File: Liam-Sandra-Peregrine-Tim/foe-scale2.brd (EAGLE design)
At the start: 96.2 x 67.3 mm, 52 parts, among them U1 LM311, U2 SAMD21E

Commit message: fixed up a couple things in board
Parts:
- added R18: 0, resistor:R0805
- moved DGND 18.0 mm to (58.4, 17.8)
- moved U$5 5.68 mm to (58.4, 36.8)
- moved U$4 2.54 mm to (64.8, 36.8)
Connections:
- net AGND: now also R18.2
- net DGND: now also R18.1
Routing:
- net +5V: track 274.7 -> 284.8 mm
- net AGND: track 65.9 -> 72.0 mm, vias 12 -> 13
- net DBG-PIN-PA14: track 5.98 -> 11.6 mm
- net DGND: track 76.8 -> 80.6 mm, vias 14 -> 15
- net RST: track 44.7 -> 44.1 mm

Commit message: pushing
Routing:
- net N$70: track 8.86 -> 11.5 mm
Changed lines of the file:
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@@
 </class>
 </classes>
-<designrules name="default">
+<designrules name="default *">
 <description language="de">&lt;b&gt;EAGLE Design Rules&lt;/b&gt;
 &lt;p&gt;
@@
 <param name="mtCopper" value="0.035mm 0.035mm 0.035mm 0.035mm 0.035mm 0.035mm 0.035mm 0.035mm 0.035mm 0.035mm 0.035mm 0.035mm 0.035mm 0.035mm 0.035mm 0.035mm"/>
 <param name="mtIsolate" value="1.5mm 0.15mm 0.2mm 0.15mm 0.2mm 0.15mm 0.2mm 0.15mm 0.2mm 0.15mm 0.2mm 0.15mm 0.2mm 0.15mm 0.2mm"/>
-<param name="mdWireWire" value="8mil"/>
-<param name="mdWirePad" value="8mil"/>
-<param name="mdWireVia" value="8mil"/>
-<param name="mdPadPad" value="8mil"/>
-<param name="mdPadVia" value="8mil"/>
-<param name="mdViaVia" value="8mil"/>
-<param name="mdSmdPad" value="8mil"/>
-<param name="mdSmdVia" value="8mil"/>
-<param name="mdSmdSmd" value="8mil"/>
+<param name="mdWireWire" value="6mil"/>
+<param name="mdWirePad" value="6mil"/>
+<param name="mdWireVia" value="6mil"/>
+<param name="mdPadPad" value="6mil"/>
+<param name="mdPadVia" value="6mil"/>
+<param name="mdViaVia" value="6mil"/>
+<param name="mdSmdPad" value="6mil"/>
+<param name="mdSmdVia" value="6mil"/>
+<param name="mdSmdSmd" value="6mil"/>
 <param name="mdViaViaSameLayer" value="8mil"/>
 <param name="mnLayersViaInSmd" value="2"/>
 <param name="mdCopperDimension" value="40mil"/>
-<param name="mdDrill" value="8mil"/>
+<param name="mdDrill" value="6mil"/>
 <param name="mdSmdStop" value="0mil"/>
 <param name="msWidth" value="10mil"/>
@@
 </element>
 <element name="R11" library="resistor" package="R0805" value="10k" x="63.5" y="76.2" smashed="yes" rot="R180">
-<attribute name="NAME" x="60.833" y="75.438" size="1.27" layer="25" rot="R270"/>
+<attribute name="NAME" x="60.671525" y="75.39493125" size="1.27" layer="25" rot="R270"/>
 <attribute name="VALUE" x="61.849" y="78.232" size="1.27" layer="27"/>
 </element>
@@
 <wire x1="37.973" y1="41.275" x2="37.846" y2="41.402" width="0.4064" layer="1"/>
 <wire x1="37.846" y1="41.402" x2="37.846" y2="42.164" width="0.4064" layer="1"/>
-<wire x1="37.846" y1="42.164" x2="35.56" y2="44.45" width="0.4064" layer="1"/>
-<wire x1="35.56" y1="44.45" x2="32.512" y2="44.45" width="0.4064" layer="1"/>
-<wire x1="32.512" y1="44.45" x2="29.718" y2="47.244" width="0.4064" layer="1"/>
+<wire x1="37.846" y1="42.164" x2="35.549234375" y2="44.633034375" width="0.4064" layer="1"/>
+<wire x1="35.549234375" y1="44.633034375" x2="32.501234375" y2="44.633034375" width="0.4064" layer="1"/>
+<wire x1="32.501234375" y1="44.633034375" x2="29.718" y2="47.244" width="0.4064" layer="1"/>
 <wire x1="29.718" y1="47.244" x2="29.718" y2="49.276" width="0.4064" layer="1"/>
 <wire x1="29.718" y1="49.276" x2="22.606" y2="56.388" width="0.4064" layer="1"/>
@@
 <contactref element="U2" pad="3"/>
 <wire x1="30.16" y1="59.69" x2="30.48" y2="59.69" width="0.4064" layer="1"/>
-<wire x1="74.86" y1="48.1076" x2="74.86" y2="46.92" width="0.4064" layer="1"/>
-<wire x1="74.86" y1="46.92" x2="73.66" y2="45.72" width="0.4064" layer="1"/>
-<via x="73.66" y="45.72" extent="1-16" drill="0.6"/>
-<wire x1="73.66" y1="45.72" x2="71.12" y2="45.72" width="0.4064" layer="16"/>
-<wire x1="71.12" y1="45.72" x2="69.088" y2="47.752" width="0.4064" layer="16"/>
+<wire x1="74.86" y1="48.1076" x2="74.816940625" y2="46.672365625" width="0.4064" layer="1"/>
+<wire x1="74.816940625" y1="46.672365625" x2="73.616940625" y2="45.472365625" width="0.4064" layer="1"/>
+<via x="73.616940625" y="45.472365625" extent="1-16" drill="0.6"/>
+<wire x1="73.616940625" y1="45.472365625" x2="71.173825" y2="45.48313125" width="0.4064" layer="16"/>
+<wire x1="71.173825" y1="45.48313125" x2="69.088" y2="47.752" width="0.4064" layer="16"/>
 <via x="69.088" y="47.752" extent="1-16" drill="0.6"/>
 <wire x1="69.088" y1="47.752" x2="68.072" y2="47.752" width="0.4064" layer="1"/>
@@
 <contactref element="R12" pad="2"/>
 <contactref element="AS1363" pad="2"/>
-<wire x1="66.04" y1="72.27" x2="66.04" y2="72.898" width="0.4064" layer="1"/>
-<wire x1="66.04" y1="72.898" x2="65.278" y2="73.66" width="0.4064" layer="1"/>
-<via x="65.278" y="73.66" extent="1-16" drill="0.6"/>
-<wire x1="65.278" y1="73.66" x2="65.278" y2="74.168" width="0.4064" layer="16"/>
+<wire x1="66.04" y1="72.27" x2="66.06233125" y2="73.724378125" width="0.4064" layer="1"/>
+<wire x1="66.06233125" y1="73.724378125" x2="64.008" y2="73.66" width="0.4064" layer="1"/>
+<via x="64.008" y="73.66" extent="1-16" drill="0.6"/>
+<wire x1="64.008" y1="73.66" x2="65.278" y2="74.168" width="0.4064" layer="16"/>
 <wire x1="65.278" y1="74.168" x2="66.04" y2="74.93" width="0.4064" layer="16"/>
 <wire x1="66.04" y1="74.93" x2="66.294" y2="76.454" width="0.4064" layer="16"/>

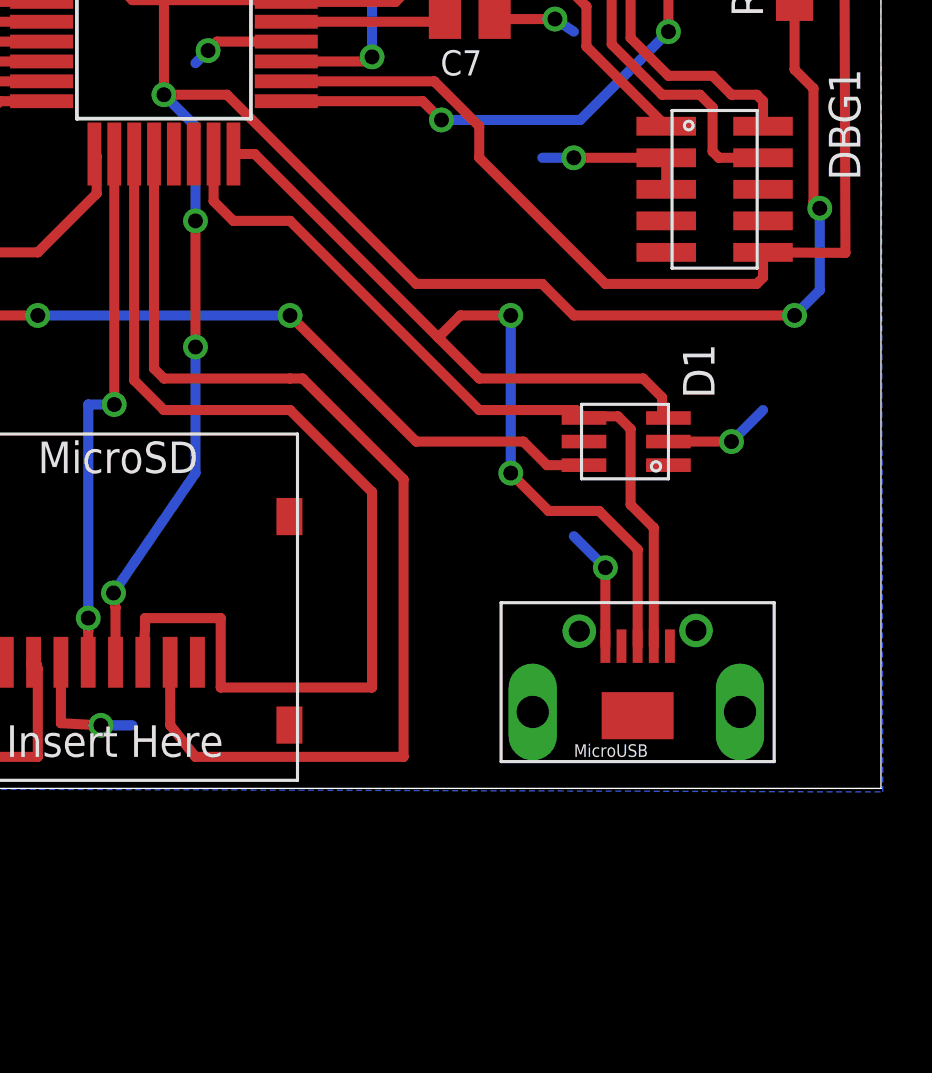
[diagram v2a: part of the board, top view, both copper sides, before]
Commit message: replaced microUSB with standard USB B
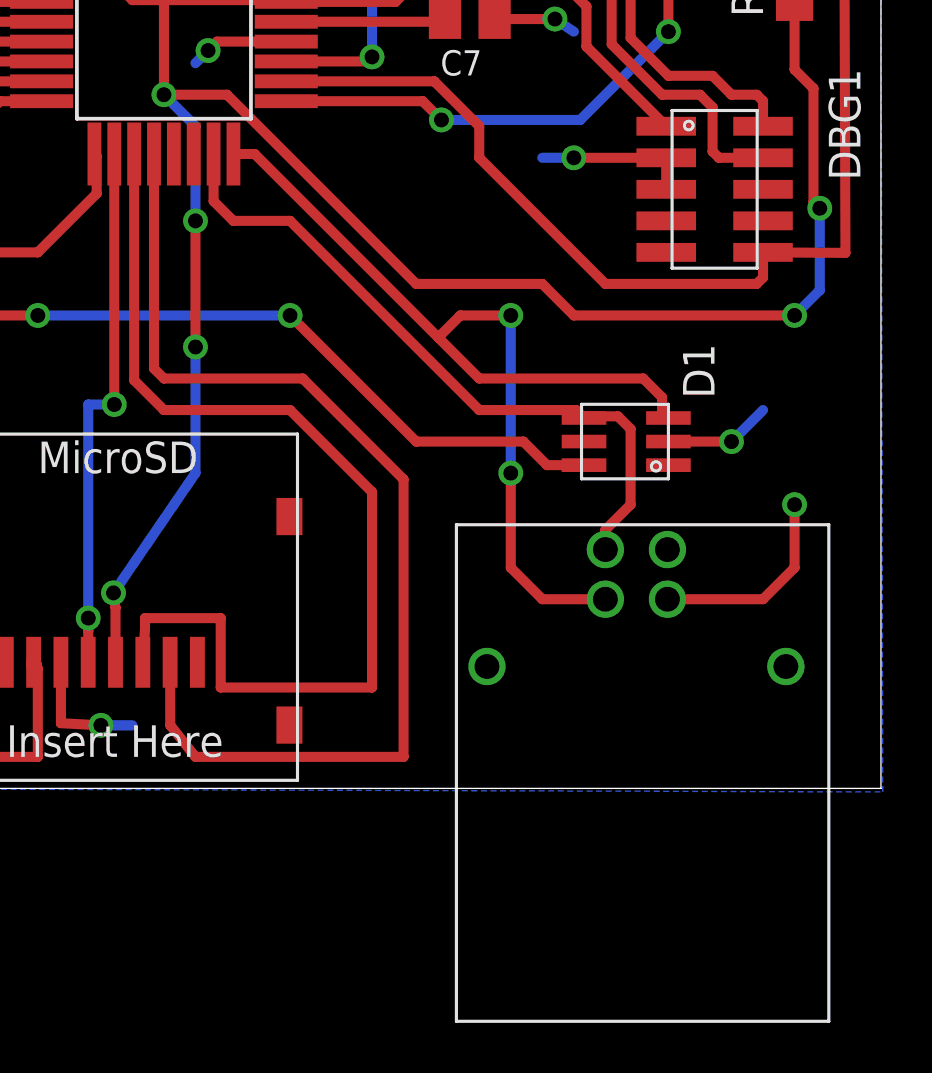
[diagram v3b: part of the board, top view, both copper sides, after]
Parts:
- U$13: value MICRO-USB-CONNECTOR -> USB-B; device foe-scale:MICRO-USB-CONNECTOR -> foe-scale:USB-B
- moved U$13 2.54 mm to (91.4, 20.3)
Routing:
- net USB_D-_PA24: track 31.7 -> 27.8 mm
- net DGND: track 80.6 -> 83.9 mm
- net USB_D+_PA25: track 42.2 -> 40.0 mm
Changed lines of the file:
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@@
 <?xml version="1.0" encoding="utf-8"?>
 <!DOCTYPE eagle SYSTEM "eagle.dtd">
-<eagle version="7.4.0">
+<eagle version="7.5.0">
 <drawing>
 <settings>
@@
 Shifter</text>
 <text x="62.23" y="16.51" size="1.778" layer="27" rot="R90">MicroSD</text>
-<text x="100.838" y="13.716" size="1.778" layer="27" rot="R90">MicroUSB</text>
+<text x="102.108" y="13.716" size="1.778" layer="27" rot="R90">MicroUSB</text>
 </plain>
 <attributes>
@@
 <element name="U$11" library="foe-scale" package="PUSHBTN" value="BUTTON_THRU" x="92.71" y="55.88" rot="R270"/>
 <element name="U$12" library="foe-scale" package="PUSHBTN" value="BUTTON_THRU" x="92.71" y="69.85" rot="R270"/>
-<element name="U$13" library="foe-scale" package="MICRO-USB-CONNECTOR" value="MICRO-USB-CONNECTOR" x="91.44" y="17.78"/>
+<element name="U$13" library="foe-scale" package="USB-B" value="USB-B" x="91.44" y="20.32"/>
 <element name="U$2" library="foe-scale" package="S8-LT1789-1" value="LT1789-1-INSTR-AMP" x="15.24" y="45.72" smashed="yes" rot="R270"/>
 <element name="U$3" library="foe-scale" package="SOIC8" value="LMC6482" x="36.83" y="41.91" smashed="yes" rot="R270">
@@
 <via x="96.52" y="26.67" extent="1-16" drill="0.6"/>
 <wire x1="96.52" y1="26.67" x2="97.79" y2="27.94" width="0.4064" layer="16"/>
-<wire x1="91.44" y1="18.43" x2="91.44" y2="21.59" width="0.4064" layer="1"/>
-<via x="91.44" y="21.59" extent="1-16" drill="0.6"/>
-<wire x1="91.44" y1="21.59" x2="90.17" y2="22.86" width="0.4064" layer="16"/>
+<via x="99.06" y="24.13" extent="1-16" drill="0.6"/>
 <wire x1="93.89" y1="36.83" x2="93.89" y2="38.1" width="0.4064" layer="1"/>
 <wire x1="93.89" y1="38.1" x2="90.17" y2="38.1" width="0.4064" layer="1"/>
@@
 <via x="58.42" y="66.04" extent="1-16" drill="0.6"/>
 <wire x1="58.42" y1="66.04" x2="58.42" y2="64.77" width="0.6096" layer="16"/>
+<wire x1="93.94" y1="20.32" x2="97.79" y2="20.32" width="0.4064" layer="1"/>
+<wire x1="97.79" y1="20.32" x2="99.06" y2="21.59" width="0.4064" layer="1"/>
+<wire x1="99.06" y1="21.59" x2="99.06" y2="24.13" width="0.4064" layer="1"/>
+<wire x1="87.63" y1="69.85" x2="97.7138" y2="74.8538" width="0" layer="19" extent="16-16"/>
+<wire x1="78.74" y1="73.66" x2="84.82" y2="68.58" width="0" layer="19" extent="1-16"/>
+<wire x1="65.09" y1="69.97" x2="74.93" y2="75.2" width="0" layer="19" extent="1-1"/>
+<wire x1="59.69" y1="67.31" x2="62.23" y2="68.58" width="0" layer="19" extent="16-16"/>
+<wire x1="58.42" y1="66.04" x2="59.69" y2="67.31" width="0" layer="19" extent="1-16"/>
+<wire x1="58.42" y1="55.88" x2="58.42" y2="64.77" width="0" layer="19" extent="16-16"/>
+<wire x1="54.035" y1="47.565" x2="56.300771875" y2="53.63770625" width="0" layer="19" extent="1-1"/>
+<wire x1="66.04" y1="45.72" x2="59.69" y2="40.64" width="0" layer="19" extent="1-16"/>
+<wire x1="74.93" y1="41.91" x2="68.7324" y2="45.18" width="0" layer="19" extent="1-16"/>
+<wire x1="86.979" y1="43.688" x2="78.5876" y2="42.78" width="0" layer="19" extent="1-1"/>
+<wire x1="90.17" y1="38.1" x2="90.17" y2="43.18" width="0" layer="19" extent="1-16"/>
+<wire x1="97.79" y1="27.94" x2="93.89" y2="36.83" width="0" layer="19" extent="1-16"/>
+<wire x1="99.06" y1="24.13" x2="96.52" y2="26.67" width="0" layer="19" extent="16-16"/>
+<wire x1="59.69" y1="29.21" x2="59.69" y2="40.64" width="0" layer="19" extent="16-16"/>
+<wire x1="58.42" y1="17.78" x2="59.0032625" y2="28.5232625" width="0" layer="19" extent="1-1"/>
+<wire x1="69.51" y1="17.78" x2="58.42" y2="17.78" width="0" layer="19" extent="1-1"/>
+<wire x1="99.06" y1="50.53" x2="90.17" y2="43.18" width="0" layer="19" extent="1-16"/>
+<wire x1="97.7138" y1="60.8838" x2="100.33" y2="54.61" width="0" layer="19" extent="16-16"/>
 </signal>
 <signal name="DO-PA16">
@@
 <contactref element="U$8" pad="CD"/>
 <contactref element="U2" pad="20"/>
-<wire x1="73.26" y1="38.2524" x2="73.26" y2="29.972" width="0.4064" layer="1"/>
-<wire x1="73.26" y1="29.972" x2="73.26" y2="29.61" width="0.4064" layer="1"/>
+<wire x1="73.26" y1="38.2524" x2="73.26" y2="29.61" width="0.4064" layer="1"/>
 <wire x1="73.26" y1="29.61" x2="73.66" y2="29.21" width="0.4064" layer="1"/>
-<wire x1="73.66" y1="29.21" x2="78.74" y2="29.21" width="0.4064" layer="1"/>
-<wire x1="78.74" y1="29.21" x2="79.248" y2="29.21" width="0.4064" layer="1"/>
+<wire x1="73.66" y1="29.21" x2="79.248" y2="29.21" width="0.4064" layer="1"/>
 <wire x1="79.248" y1="29.21" x2="83.312" y2="25.146" width="0.4064" layer="1"/>
 <wire x1="83.312" y1="25.146" x2="83.312" y2="13.97" width="0.4064" layer="1"/>
@@
 <wire x1="86.36" y1="27.94" x2="90.26" y2="27.94" width="0.4064" layer="1"/>
 <wire x1="90.26" y1="27.94" x2="90.58" y2="27.62" width="0.4064" layer="1"/>
-<wire x1="93.39" y1="18.43" x2="93.39" y2="23.196" width="0.4064" layer="1"/>
-<wire x1="93.39" y1="23.196" x2="92.456" y2="24.13" width="0.4064" layer="1"/>
 <wire x1="92.456" y1="24.13" x2="92.456" y2="27.178" width="0.4064" layer="1"/>
 <wire x1="92.456" y1="27.178" x2="91.948" y2="27.686" width="0.4064" layer="1"/>
 <wire x1="91.948" y1="27.686" x2="90.646" y2="27.686" width="0.4064" layer="1"/>
 <wire x1="90.646" y1="27.686" x2="90.58" y2="27.62" width="0.4064" layer="1"/>
+<wire x1="91.44" y1="22.32" x2="91.44" y2="23.114" width="0.4064" layer="1"/>
+<wire x1="91.44" y1="23.114" x2="92.456" y2="24.13" width="0.4064" layer="1"/>
 </signal>
 <signal name="USB_D+_PA25">
@@
 <wire x1="93.726" y1="28.448" x2="93.726" y2="27.874" width="0.4064" layer="1"/>
 <wire x1="93.726" y1="27.874" x2="93.98" y2="27.62" width="0.4064" layer="1"/>
-<wire x1="92.74" y1="18.43" x2="92.74" y2="22.322" width="0.4064" layer="1"/>
-<wire x1="92.74" y1="22.322" x2="91.186" y2="23.876" width="0.4064" layer="1"/>
-<wire x1="91.186" y1="23.876" x2="89.154" y2="23.876" width="0.4064" layer="1"/>
-<wire x1="89.154" y1="23.876" x2="87.63" y2="25.4" width="0.4064" layer="1"/>
 <via x="87.63" y="25.4" extent="1-16" drill="0.6"/>
 <wire x1="87.63" y1="25.4" x2="87.63" y2="31.75" width="0.4064" layer="16"/>
@@
 <wire x1="87.63" y1="31.75" x2="85.598" y2="31.75" width="0.4064" layer="1"/>
 <wire x1="85.598" y1="31.75" x2="84.709" y2="30.861" width="0.4064" layer="1"/>
+<wire x1="91.44" y1="20.32" x2="88.9" y2="20.32" width="0.4064" layer="1"/>
+<wire x1="88.9" y1="20.32" x2="87.63" y2="21.59" width="0.4064" layer="1"/>
+<wire x1="87.63" y1="21.59" x2="87.63" y2="25.4" width="0.4064" layer="1"/>
 </signal>
 <signal name="N$45">
